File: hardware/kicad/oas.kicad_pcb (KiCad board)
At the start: 2 copper layers, 120 x 103.5 mm, 69 parts, among them J1 Phoenix_MSTBA_2,5/3-G-5,08 (2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, J10 Native-USB recovery (DNP), J2 UART/Boot Recovery (DNP), J3 JST SM06B-GHS-TB (SEN66 conne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, J4 1x5 P1.27mm header (HLK-LD241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, J5 ESP32 row A (pins 1..15, ante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, J6 ESP32 row B (pins 16..30, USB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, J7 MIKROE mikroBUS pins 1..8 (AN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, J8 MIKROE mikroBUS pins 9..16 (P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, J9 JST SM04B-SRSS-TB (Qwiic / St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, Q1 AO3401A, SW1 C&K PTS645VK392LFS, U1 LM2596S-5.0, U2 TPS62933

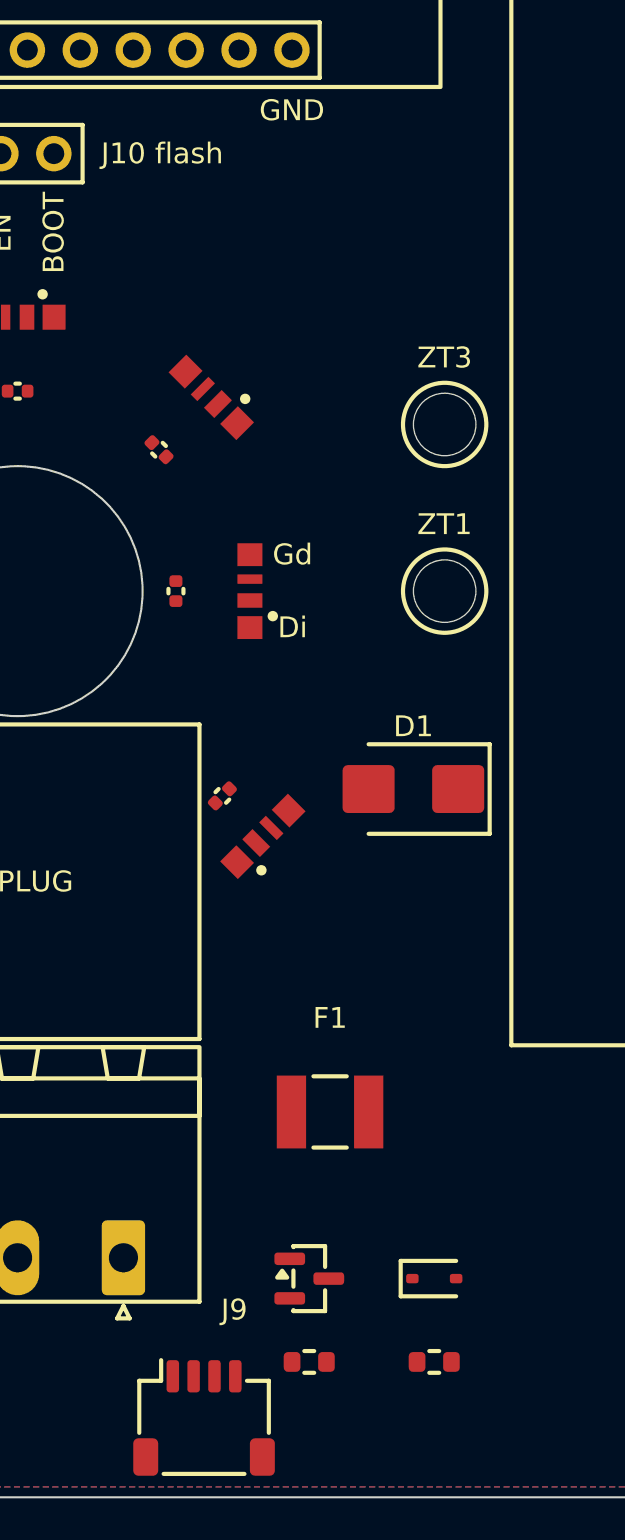
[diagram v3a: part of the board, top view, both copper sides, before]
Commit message: refactor(placement): de-congest the J1/Q1 corner — cluster spread + J9 internal + C2 removed
Placement-only checkpoint (no routing): every component move needed for a
clean re-route, verified DFM-clean BEFORE any trace is laid. This is the
de-congested baseline the autoroute proceeds from.

- J9 (Qwiic) relocated from the C2 chord-side wall cutout to an internal
  position east of J10 (+17.0, -19.5). An external Qwiic cable from a
  sealed enclosure conflicts with design Pillar #2; a future-expansion
  port is realistically internal. A direct "J9" F.SilkS label replaces
  the old C2-cutout silk label.
- C2 cutout removed entirely from CUTOUTS (+ its silk). It only hosted
  J9; an empty case-wall keepout sterilises routing space and — the root
  cause that defeated three prior routing attempts — exported to
  Freerouting as a HARD keepout that trapped the protection cluster pads.
- J1/Q1 reverse-polarity protection cluster (Q1/F1/R4/R1/D1/D3) spread
  across the full corridor instead of jammed courtyard-to-courtyard, so
  traces can escape the pad areas.
- U1 (LM2596S buck): a 180° rotation was evaluated to relieve buck
  fan-out congestion but does not fit — the flip swings the TO-263-5
  lead row into the ESP32 body silk and the compensating westward shift
  collides with LD2410 (the corridor is 15.7 mm). Kept at rotation 0.

ROUTING_CHUNKS stays ("gnd",) — the autoroute is the next step from here.

build.py 30/30 PASS. DRC 0, ERC 0, determinism 20/20.
JLCDFM: 0 Danger / 0 Warning (PCB + SMT).

Co-Authored-By: Claude Opus 4.7 <noreply@anthropic.com>
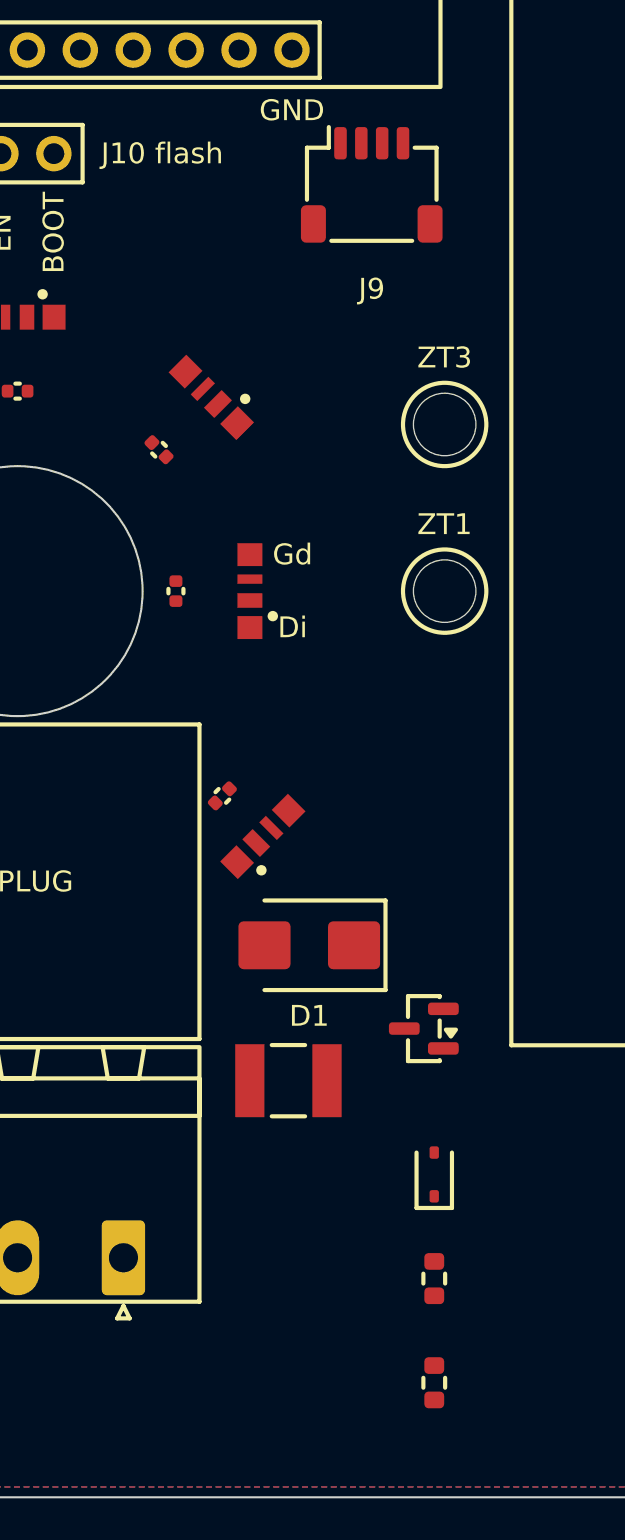
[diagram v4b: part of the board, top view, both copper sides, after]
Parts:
- moved J9 59.7 mm to (165.5, 85.5)
- moved Q1 13.2 mm to (168.0, 126.0), turned to 180 degrees
- moved D1 9.01 mm to (162.5, 122.0)
- moved R1 6.08 mm to (168.5, 143.0), turned to 90 degrees
- moved D3 5.00 mm to (168.5, 133.0), turned to 90 degrees
- moved R4 4.00 mm to (168.5, 138.0), turned to 90 degrees
- moved F1 2.50 mm to (161.5, 128.5)
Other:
- board text removed: "C2 15.7×16.3"
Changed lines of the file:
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@@
 )
 (gr_rect
-	(start 149.6 132.198)
-	(end 165.3 148.497798)
-	(stroke (width 0.1) (type solid))
-	(fill no)
-	(layer "Dwgs.User")
-)
-(gr_text "C2\n15.7×16.3"
-	(at 157.45 140.347899)
-	(layer "Dwgs.User")
-	(effects
-		(font (size 0.8 0.8) (thickness 0.12))
-	)
-)
-(gr_rect
 	(start 135.5 132.198)
 	(end 146.5 148.497798)
@@
 (footprint "Connector_JST:JST_SH_SM04B-SRSS-TB_1x04-1MP_P1.00mm_Horizontal"
 	(layer "F.Cu")
-	(at 157.45 144.69 0)
+	(at 165.5 85.5 0)
 (property "Reference" "J9"
 	(at 0 -3.6 0)
@@
 (footprint "Diode_SMD:D_SMB"
 	(layer "F.Cu")
-	(at 167.5 114.5 180)
+	(at 162.5 122 180)
 (property "Reference" "D1"
 	(at 0 -3.1 180)
@@
 (footprint "Package_TO_SOT_SMD:SOT-23"
 	(layer "F.Cu")
-	(at 162.5 138 0)
+	(at 168 126 180)
 (property "Reference" "Q1"
-	(at 0 -2.4 0)
+	(at 0 -2.4 180)
 	(layer "F.SilkS")
 			(hide yes)
@@
 )
 (property "Value" "AO3401A"
-	(at 0 2.4 0)
+	(at 0 2.4 180)
 	(layer "F.Fab")
 			(hide yes)
@@
 		)
 	(pad "1" smd roundrect
-			(at -0.9375 -0.95)
+			(at -0.9375 -0.95 180)
 			(size 1.475 0.6)
 			(layers "F.Cu" "F.Mask" "F.Paste")
@@
 		)
 	(pad "2" smd roundrect
-			(at -0.9375 0.95)
+			(at -0.9375 0.95 180)
 			(size 1.475 0.6)
 			(layers "F.Cu" "F.Mask" "F.Paste")
@@
 		)
 	(pad "3" smd roundrect
-			(at 0.9375 0)
+			(at 0.9375 0 180)
 			(size 1.475 0.6)
 			(layers "F.Cu" "F.Mask" "F.Paste")
@@
 (footprint "Diode_SMD:D_SOD-323"
 	(layer "F.Cu")
-	(at 168.5 138 0)
+	(at 168.5 133 90)
 (property "Reference" "D3"
-	(at 0 -1.5 0)
+	(at 0 -1.5 90)
 	(layer "F.SilkS")
 			(hide yes)
@@
 )
 (property "Value" "10V Zener 200mW"
-	(at 0 1.5 0)
+	(at 0 1.5 90)
 	(layer "F.Fab")
 			(hide yes)
@@
 		)
 	(pad "1" smd roundrect
-			(at -1.05 0)
+			(at -1.05 0 90)
 			(size 0.6 0.45)
 			(layers "F.Cu" "F.Mask" "F.Paste")
@@
 		)
 	(pad "2" smd roundrect
-			(at 1.05 0)
+			(at 1.05 0 90)
 			(size 0.6 0.45)
 			(layers "F.Cu" "F.Mask" "F.Paste")
@@
         	(footprint "oas:Fuse_1812L_4532Metric"
         		(layer "F.Cu")
-        		(at 163.5 130 0)
+        		(at 161.5 128.5 0)
         		(descr "PTC polyfuse 750 mA hold / 1.5 A trip / 33 V (Littelfuse 1812L075/33DR, LCSC C151170, 1812 SMD).")
         		(attr smd)
@@
 (footprint "Resistor_SMD:R_0603_1608Metric"
 	(layer "F.Cu")
-	(at 162.5 142 0)
-(property "Reference" "R1"
-	(at 0 -1.45 0)
+	(at 168.5 138 90)
+(property "Reference" "R4"
+	(at 0 -1.45 90)
 	(layer "F.SilkS")
 			(hide yes)
 	(effects (font (size 1 1) (thickness 0.2)))
 )
-(property "Value" "100k 1%"
-	(at 0 1.45 0)
+(property "Value" "1k"
+	(at 0 1.45 90)
 	(layer "F.Fab")
 			(hide yes)
@@
 	(effects (font (size 1.27 1.27)))
 )
-(property "Description" "100 kΩ 1% gate-GND pulldown for Q1 (P-MOSFET reverse-polarity)."
+(property "Description" "1 kΩ gate series resistor between Q1.G and Vgs clamp junction."
 	(at 0 0 0)
 	(layer "F.Fab")
@@
 			(layer "F.Fab")
 		)
-	(fp_text user "R1"
+	(fp_text user "R4"
 			(at 0 0 0)
 			(layer "F.Fab")
@@
 		)
 	(pad "1" smd roundrect
-			(at -0.825 0)
+			(at -0.825 0 90)
 			(size 0.8 0.95)
 			(layers "F.Cu" "F.Mask" "F.Paste")
 			(roundrect_rratio 0.25)
-			(net 20 "Net-(D3-A)")
+			(net 28 "Net-(Q1-G)")
 		)
 	(pad "2" smd roundrect
-			(at 0.825 0)
+			(at 0.825 0 90)
 			(size 0.8 0.95)
 			(layers "F.Cu" "F.Mask" "F.Paste")
 			(roundrect_rratio 0.25)
-			(net 17 "GND")
+			(net 20 "Net-(D3-A)")
 		)
 	(model "${KICAD10_3DMODEL_DIR}/Resistor_SMD.3dshapes/R_0603_1608Metric.step"
@@
 (footprint "Resistor_SMD:R_0603_1608Metric"
 	(layer "F.Cu")
-	(at 168.5 142 0)
-(property "Reference" "R4"
-	(at 0 -1.45 0)
+	(at 168.5 143 90)
+(property "Reference" "R1"
+	(at 0 -1.45 90)
 	(layer "F.SilkS")
 			(hide yes)
 	(effects (font (size 1 1) (thickness 0.2)))
 )
-(property "Value" "1k"
-	(at 0 1.45 0)
+(property "Value" "100k 1%"
+	(at 0 1.45 90)
 	(layer "F.Fab")
 			(hide yes)
@@
 	(effects (font (size 1.27 1.27)))
 )
-(property "Description" "1 kΩ gate series resistor between Q1.G and Vgs clamp junction."
+(property "Description" "100 kΩ 1% gate-GND pulldown for Q1 (P-MOSFET reverse-polarity)."
 	(at 0 0 0)
 	(layer "F.Fab")
@@
 			(layer "F.Fab")
 		)
-	(fp_text user "R4"
+	(fp_text user "R1"
 			(at 0 0 0)
 			(layer "F.Fab")
@@
 		)
 	(pad "1" smd roundrect
-			(at -0.825 0)
+			(at -0.825 0 90)
 			(size 0.8 0.95)
 			(layers "F.Cu" "F.Mask" "F.Paste")
 			(roundrect_rratio 0.25)
-			(net 28 "Net-(Q1-G)")
+			(net 20 "Net-(D3-A)")
 		)
 	(pad "2" smd roundrect
-			(at 0.825 0)
+			(at 0.825 0 90)
 			(size 0.8 0.95)
 			(layers "F.Cu" "F.Mask" "F.Paste")
 			(roundrect_rratio 0.25)
-			(net 20 "Net-(D3-A)")
+			(net 17 "GND")
 		)
 	(model "${KICAD10_3DMODEL_DIR}/Resistor_SMD.3dshapes/R_0603_1608Metric.step"
@@
 	(effects (font (size 1.27 1.27)))
 )
-(property "Description" "LM2596S-5.0 5 V 3 A asynchronous step-down buck (TI), TO-263-5. Rework 5: +1 mm east (was -36 → -35). U1 body half_x=5.3 so body now spans X ∈ [-40.3, -29.7]: 3.17 mm gap to LD2410 east edge (-43.47), 1.94 mm gap to ESP32 west edge (-27.76)."
+(property "Description" "LM2596S-5.0 5 V 3 A asynchronous step-down buck (TI), TO-263-5. Rework 5: +1 mm east (was -36 → -35). U1 body half_x=5.3 so body now spans X ∈ [-40.3, -29.7]: 3.17 mm gap to LD2410 east edge (-43.47), 1.94 mm gap to ESP32 west edge (-27.76). v0.50-rework: a 180° rotation was evaluated to relieve buck fan-out congestion but does not fit — the flip swings the 5-lead row ~8.2 mm east into the ESP32 (MOD1) body silk, and the compensating westward shift would collide with LD2410. The LD2410↔ESP32 corridor (15.7 mm) is too tight; kept at rotation 0."
 	(at 0 0 0)
 	(layer "F.Fab")
@@
 )
 (gr_text "J9 GND"
-	(at 158.95 144.69 0)
+	(at 167 85.5 0)
 	(layer "F.Fab")
 	(effects
@@
 	)
 )
+(gr_text "J9"
+	(at 165.5 90.5 0)
+	(layer "F.SilkS")
+	(effects
+		(font (size 1 1) (thickness 0.2))
+	)
+)
 (gr_text "GND"
 	(at 137.54 87.8 90)
@@
 	)
 )
-(gr_text "J9"
-	(at 158.9 139.5 0)
-	(layer "F.SilkS")
-	(effects
-		(font (size 1 1) (thickness 0.2))
-	)
-)
 (gr_text "SW1"
 	(at 141 140.8 0)
@@
 )
 (gr_text "D1"
-	(at 167.5 111.5 0)
+	(at 162.5 125.4 0)
 	(layer "F.SilkS")
 	(effects
@@
 )
 (gr_text "F1"
-	(at 163.5 125.5 0)
-	(layer "F.SilkS")
+	(at 165.2 128.5 90)
+	(layer "F.Fab")
 	(effects
-		(font (size 1 1) (thickness 0.2))
+		(font (size 1 1) (thickness 0.15))
 	)
 )
 (gr_text "Q1"
-	(at 164.75 138 90)
+	(at 168 129 0)
 	(layer "F.Fab")
 	(effects
@@
 )
 (gr_text "D3"
-	(at 171 138 0)
+	(at 170.8 133 0)
 	(layer "F.Fab")
 	(effects
@@
 	)
 )
-(gr_text "R1"
-	(at 159.5 142 0)
+(gr_text "R4"
+	(at 170.8 138 0)
 	(layer "F.Fab")
 	(effects
@@
 	)
 )
-(gr_text "R4"
-	(at 171.5 142 0)
+(gr_text "R1"
+	(at 170.8 143 0)
 	(layer "F.Fab")
 	(effects
@@
 	)
 )
-(zone
-	(net 0)
-	(net_name "")
-	(layers "F.Cu" "B.Cu")
-	(name "Connector_Cutout_C2")
-	(hatch edge 0.508)
-	(connect_pads
-		(clearance 0.508)
-	)
-	(min_thickness 0.254)
-	(filled_areas_thickness no)
-	(keepout
-		(tracks allowed)
-		(vias allowed)
-		(pads allowed)
-		(copperpour allowed)
-		(footprints allowed)
-	)
-	(placement
-		(enabled no)
-		(sheetname "")
-	)
-	(fill
-		(thermal_gap 0.508)
-		(thermal_bridge_width 0.508)
-	)
-	(polygon
-		(pts
-			(xy 149.6 132.198)
-			(xy 165.3 132.198)
-			(xy 165.3 148.497798)
-			(xy 149.6 148.497798)
-		)
-	)
-)

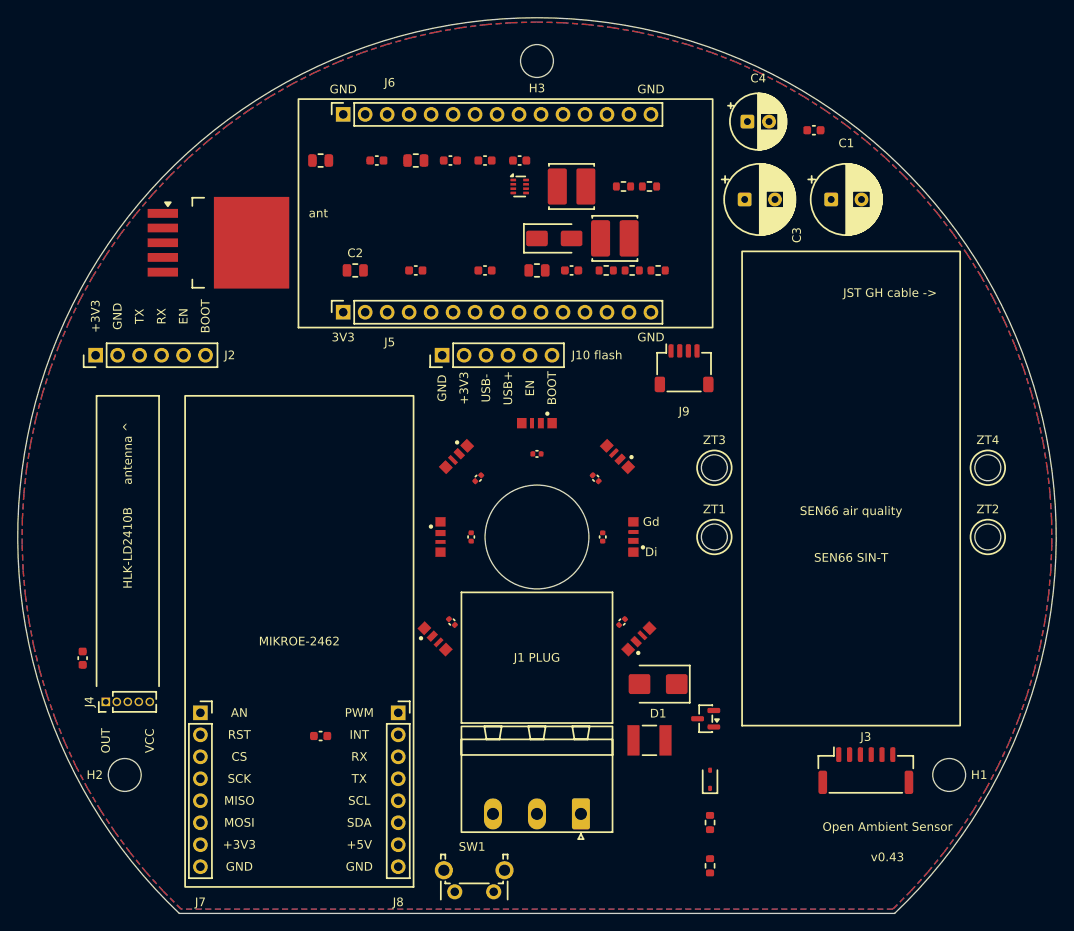
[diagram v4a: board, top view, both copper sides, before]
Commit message: refactor(placement): transcribe hand-placed buck section — U1 180°, U2/L2/Q1 moved
User hand-placed six power-section parts in KiCad to de-congest the buck
fan-out ahead of the autoroute; this transcribes those moves back into the
boardgen source of truth (placement calls + COMPONENT_ANCHORS).

- U1 (LM2596S): rotated 180° and shifted ~3 mm west to (-38.03, -34.014).
  The flip points the 5-lead row east into the ESP32 fan-out zone; the
  westward shift keeps the body clear of the LD2410 east edge. DRC clean
  (no silk_over_copper) — the v0.50 "180° does not fit" note is superseded.
- U2 (TPS62933): (-6.76, -39.25).
- L2 (2.2 µH): (+5.438, -40.5).
- Q1 (AO3401A): +2.5 mm south to (+19.438, +23.5).
- R2 / R3 (FB divider): the hand-placed spots collided — L2 overlapped R3
  (a +3V3/GND short) and R2 overlapped D2. Re-placed as a clean vertical
  0603 stack between U2 and L2 at x=-1.5 (R2 -38.0, R3 -40.5).

ROUTING_CHUNKS stays ("gnd",) — full autoroute is the next step from here.

build.py 30/30 PASS. DRC 0, ERC 0, determinism 20/20.

Co-Authored-By: Claude Opus 4.7 <noreply@anthropic.com>
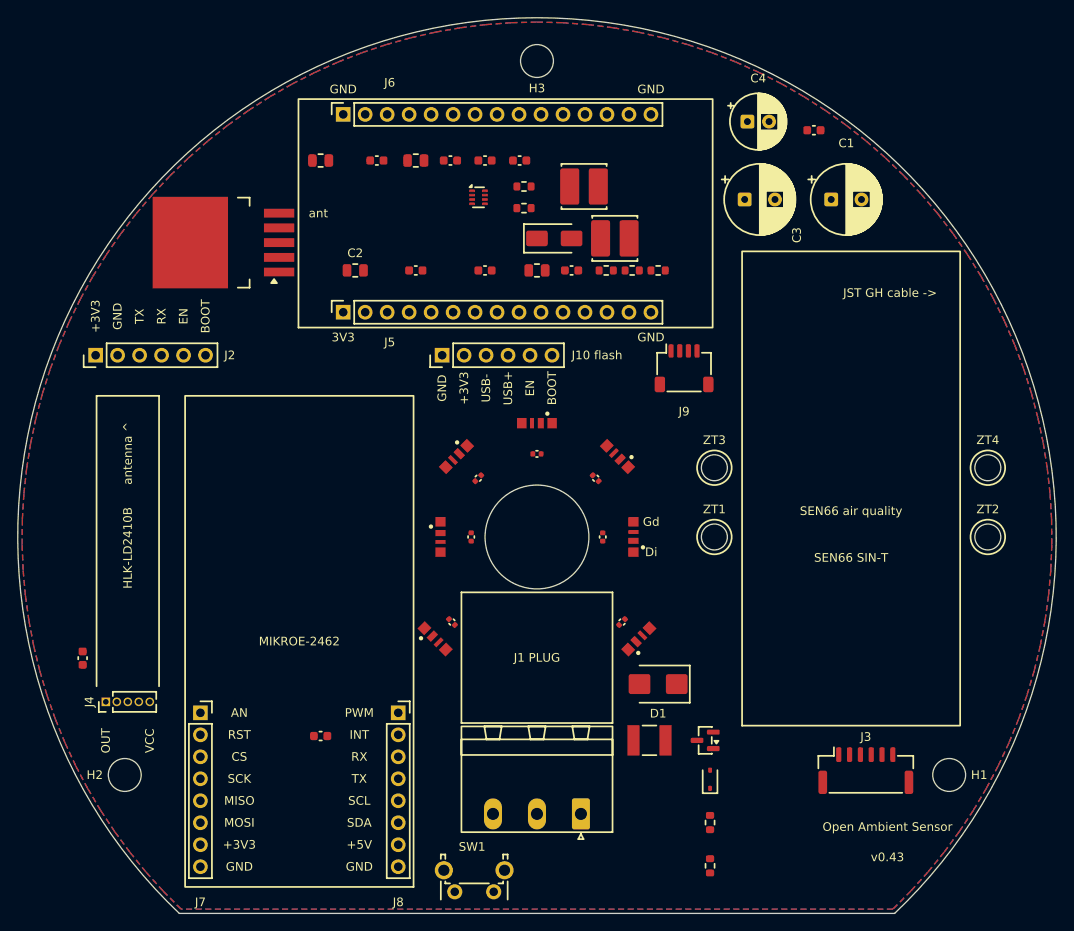
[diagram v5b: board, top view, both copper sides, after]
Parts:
- moved R3 14.5 mm to (147.0, 64.5)
- moved R2 11.8 mm to (147.0, 67.0)
- moved U2 4.92 mm to (141.7, 65.8)
- moved U1 3.03 mm to (110.5, 71.0), turned to 180 degrees
- moved Q1 2.50 mm to (167.9, 128.5)
- moved L2 1.44 mm to (153.9, 64.5)
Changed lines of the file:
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@@
 (footprint "Package_TO_SOT_SMD:SOT-23"
 	(layer "F.Cu")
-	(at 168 126 180)
+	(at 167.938 128.5 180)
 (property "Reference" "Q1"
 	(at 0 -2.4 180)
@@
 (footprint "oas:TO-263-5_LM2596"
 	(layer "F.Cu")
-	(at 113.5 71 0)
+	(at 110.47 70.986 180)
 (property "Reference" "U1"
-	(at 0 -6.65 0)
+	(at 0 -6.65 180)
 	(layer "F.SilkS")
 			(hide yes)
@@
 )
 (property "Value" "LM2596S-5.0"
-	(at 0 6.65 0)
+	(at 0 6.65 180)
 	(layer "F.Fab")
 			(hide yes)
@@
 	(effects (font (size 1.27 1.27)))
 )
-(property "Description" "LM2596S-5.0 5 V 3 A asynchronous step-down buck (TI), TO-263-5. Rework 5: +1 mm east (was -36 → -35). U1 body half_x=5.3 so body now spans X ∈ [-40.3, -29.7]: 3.17 mm gap to LD2410 east edge (-43.47), 1.94 mm gap to ESP32 west edge (-27.76). v0.50-rework: a 180° rotation was evaluated to relieve buck fan-out congestion but does not fit — the flip swings the 5-lead row ~8.2 mm east into the ESP32 (MOD1) body silk, and the compensating westward shift would collide with LD2410. The LD2410↔ESP32 corridor (15.7 mm) is too tight; kept at rotation 0."
+(property "Description" "LM2596S-5.0 5 V 3 A asynchronous step-down buck (TI), TO-263-5. v0.50-routing-rework: hand-placed in KiCad — rotated 180° and shifted ~3 mm west to (-38.03, -34.014) to relieve buck fan-out congestion. The 180° flip points the 5-lead row east toward the ESP32 fan-out zone; the compensating westward shift keeps the body clear of the LD2410 east edge."
 	(at 0 0 0)
 	(layer "F.Fab")
@@
 		)
 	(pad "1" smd rect
-			(at -8.23 -3.4)
+			(at -8.23 -3.4 180)
 			(size 3.5 1.02)
 			(layers "F.Cu" "F.Mask" "F.Paste")
@@
 		)
 	(pad "2" smd rect
-			(at -8.23 -1.7)
+			(at -8.23 -1.7 180)
 			(size 3.5 1.02)
 			(layers "F.Cu" "F.Mask" "F.Paste")
@@
 		)
 	(pad "3" smd rect
-			(at -8.23 0)
+			(at -8.23 0 180)
 			(size 3.5 1.02)
 			(layers "F.Cu" "F.Mask" "F.Paste")
@@
 		)
 	(pad "3" smd rect
-			(at 2.022 0)
+			(at 2.022 0 180)
 			(size 8.705 10.587)
 			(layers "F.Cu" "F.Mask" "F.Paste")
@@
 		)
 	(pad "4" smd rect
-			(at -8.23 1.7)
+			(at -8.23 1.7 180)
 			(size 3.5 1.02)
 			(layers "F.Cu" "F.Mask" "F.Paste")
@@
 		)
 	(pad "5" smd rect
-			(at -8.23 3.4)
+			(at -8.23 3.4 180)
 			(size 3.5 1.02)
 			(layers "F.Cu" "F.Mask" "F.Paste")
@@
 (footprint "Package_TO_SOT_SMD:SOT-583-8"
 	(layer "F.Cu")
-	(at 146.5 64.5 0)
+	(at 141.74 65.75 0)
 (property "Reference" "U2"
 	(at 0 -1.8 0)
@@
 (footprint "Inductor_SMD:L_Cenker_CKCS5040"
 	(layer "F.Cu")
-	(at 152.5 64.5 0)
+	(at 153.938 64.5 0)
 (property "Reference" "L2"
 	(at 0 -3.6 0)
@@
 (footprint "Resistor_SMD:R_0603_1608Metric"
 	(layer "F.Cu")
-	(at 158.5 64.5 0)
+	(at 147 67 0)
 (property "Reference" "R2"
 	(at 0 -1.45 0)
@@
 (footprint "Resistor_SMD:R_0603_1608Metric"
 	(layer "F.Cu")
-	(at 161.5 64.5 0)
+	(at 147 64.5 0)
 (property "Reference" "R3"
 	(at 0 -1.45 0)
@@
 )
 (gr_text "Q1"
-	(at 168 129 0)
+	(at 167.938 131.5 0)
 	(layer "F.Fab")
 	(effects
@@
 )
 (gr_text "U1"
-	(at 113.5 78 0)
+	(at 110.47 77.986 0)
 	(layer "F.Fab")
 	(effects
@@
 )
 (gr_text "U2"
-	(at 146.5 62 0)
+	(at 141.74 63.25 0)
 	(layer "F.Fab")
 	(effects
@@
 )
 (gr_text "L2"
-	(at 152.5 60.5 0)
+	(at 153.938 60.5 0)
 	(layer "F.Fab")
 	(effects
@@
 )
 (gr_text "R2"
-	(at 158.5 62.5 0)
+	(at 147 65 0)
 	(layer "F.Fab")
 	(effects
@@
 )
 (gr_text "R3"
-	(at 161.5 62.5 0)
+	(at 147 62.5 0)
 	(layer "F.Fab")
 	(effects
